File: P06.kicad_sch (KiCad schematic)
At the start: 39 parts

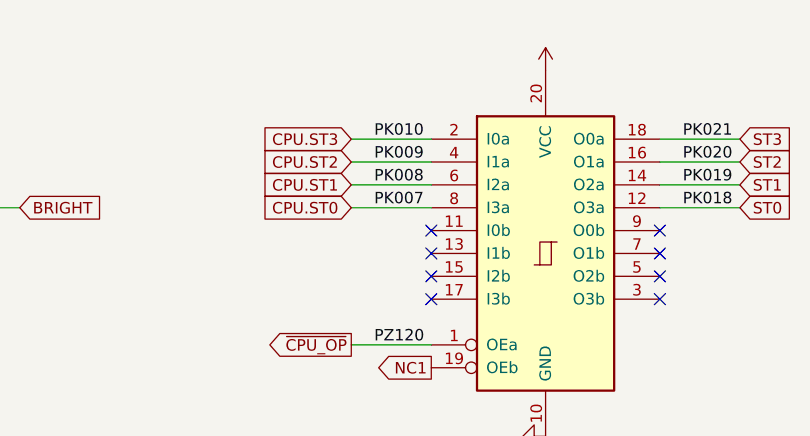
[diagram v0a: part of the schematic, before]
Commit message: fixing KiCad6 warnings
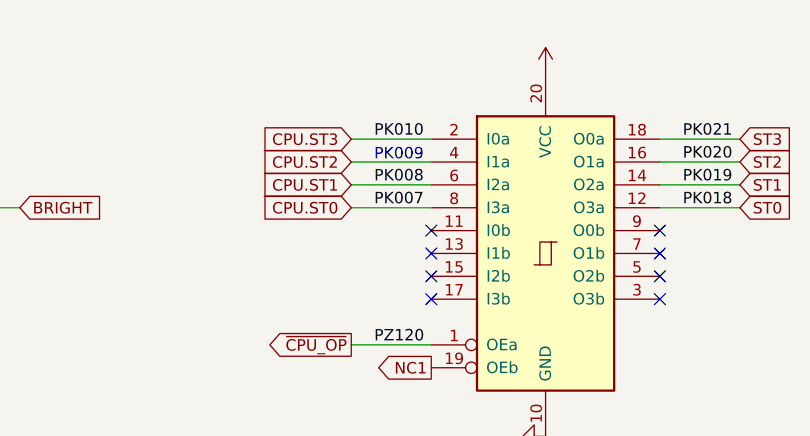
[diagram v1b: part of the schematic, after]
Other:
- note added: "PK009"
